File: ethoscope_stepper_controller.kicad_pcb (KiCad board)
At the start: 2 copper layers, 74.9 x 74.9 mm, 69 parts, among them P1 PWR_JACK_2.1x5.5_SMD_VERT, T1 TERM_BLK, T2 TERM_BLK, T3 TERM_BLK, T4 TERM_BLK, T5 TERM_BLK, T6 TERM_BLK, T7 TERM_BLK, U1 TMC429, U10 DRV8846, U11 TMC429, U12 BUFFER_TRI_STATE, U13 DRV8846, U2 BUFFER_TRI_STATE, U3 DRV8846, U4 DRV8846, U5 DRV8846, U6 TMC429, U7 BUFFER_TRI_STATE, U8 DRV8846, U9 DRV8846

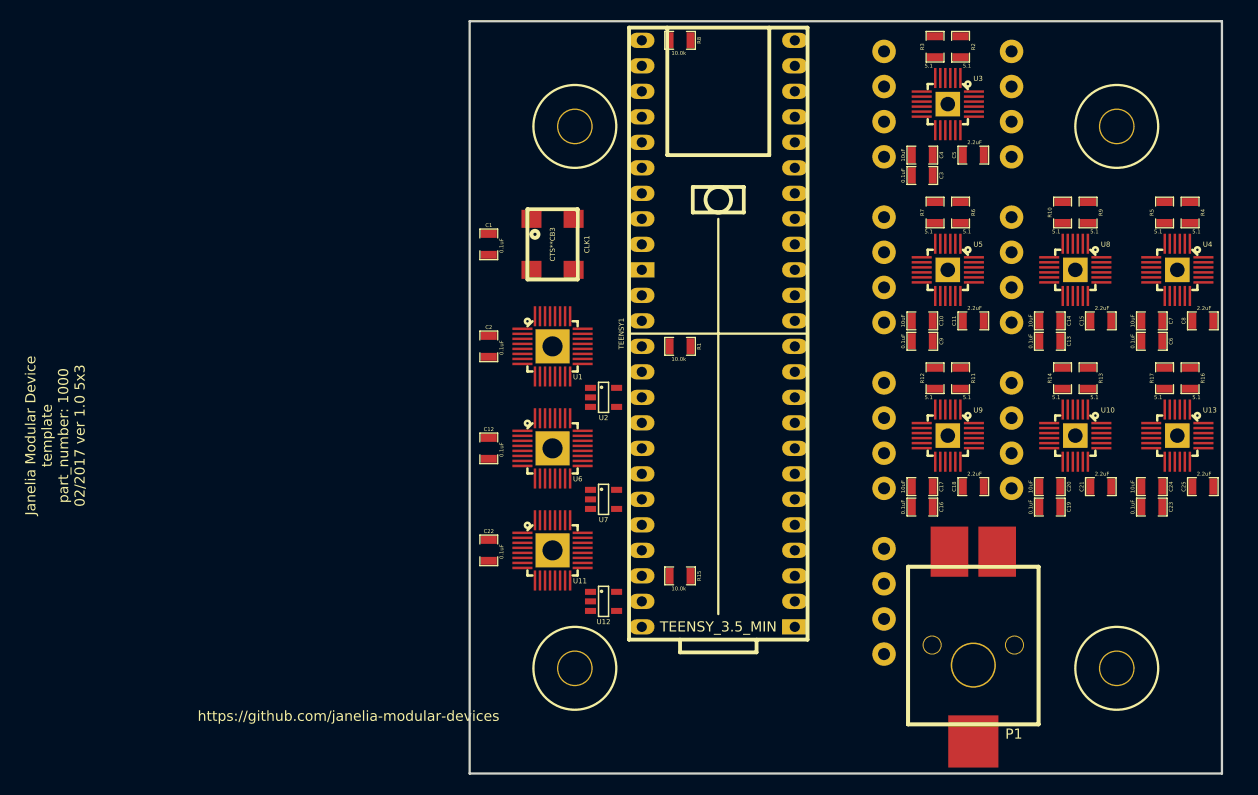
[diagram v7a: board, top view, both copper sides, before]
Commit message: Use 0402 parts when possible.
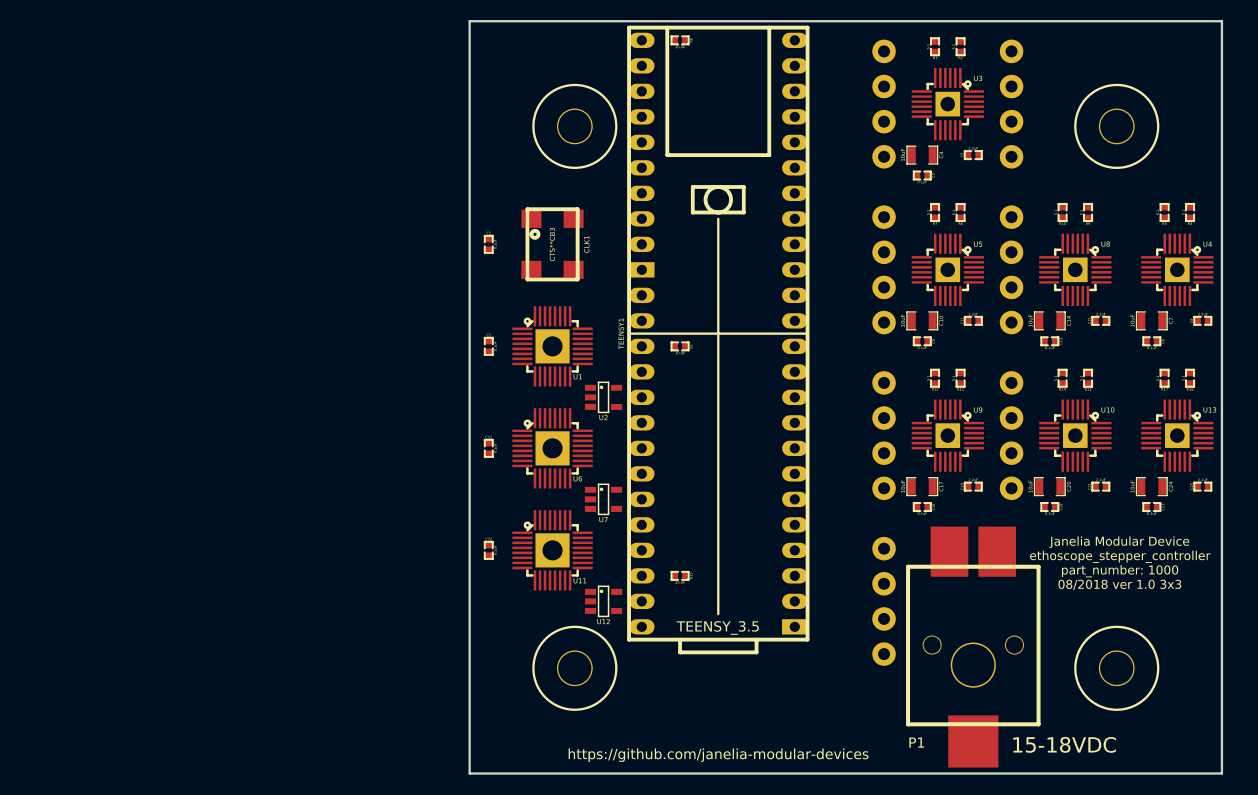
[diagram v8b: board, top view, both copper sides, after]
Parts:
- C1, C11, C12, C13, C15, C16, C18, C19, C2, C21, C22, C23, C25, C3, C5, C6, C8, C9, R1, R10, R11, R12, R13, R14, R15, R16, R17, R2, R3, R4, R5, R6, R7, R8, R9: footprint ethoscope_stepper_controller:SM0805 -> ethoscope_stepper_controller:SM0402
- TEENSY1: value TEENSY_3.5_MIN -> TEENSY_3.5
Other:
- board text added: "Janelia Modular Device ethoscope_stepper_controller part_number: 1000 08/2018 ver 1.0 3x3"
- board text removed: "Janelia Modular Device template part_number: 1000 02/2017 ver 1.0 5x3"
